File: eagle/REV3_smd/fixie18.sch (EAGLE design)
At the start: 60 parts, among them IC1 74LS595D, IC2 74LS595D, IC3 MEGA8-AI, Q1 CSTCR6M00G53Z

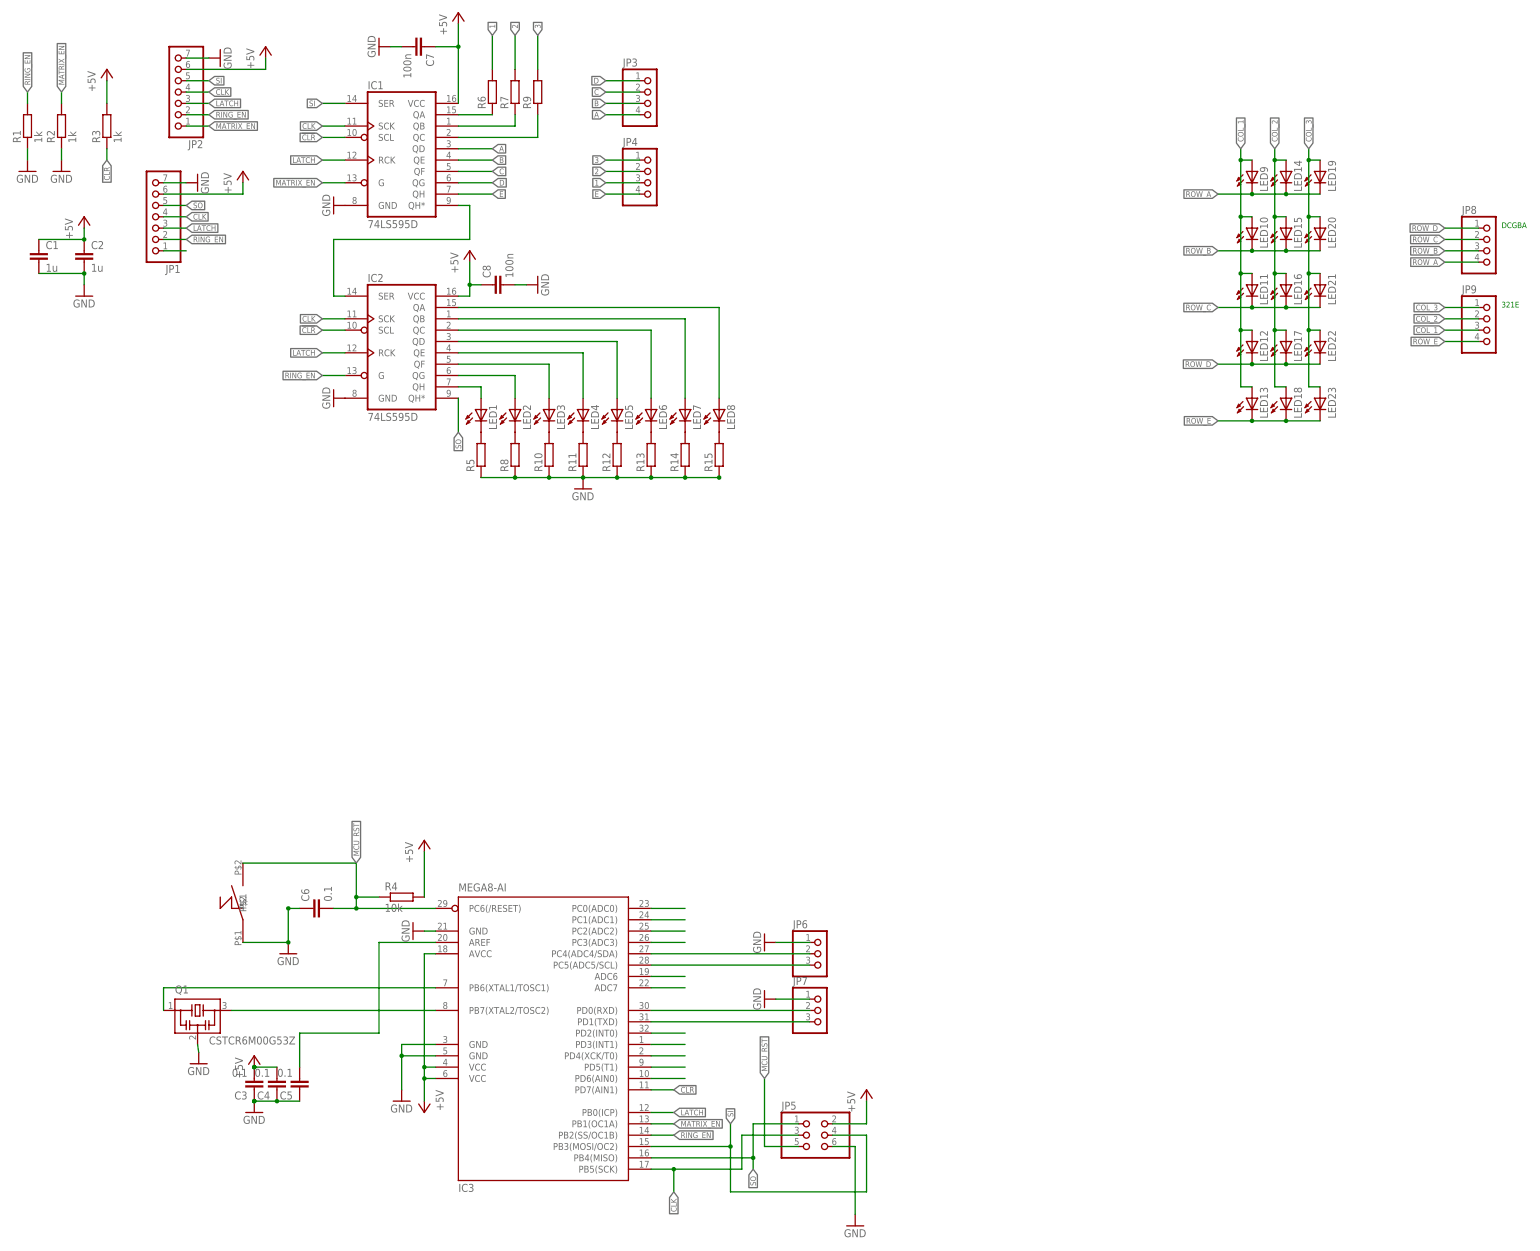
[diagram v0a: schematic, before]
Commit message: Full Rev3 Version by Alex
Used the unfinished rev3 Version to build a one 5x5cm PCB Version. With
some additional Features: second shift-register for Ring LEDs, optional
ATmega8/328 to control one or multiple PCBs.
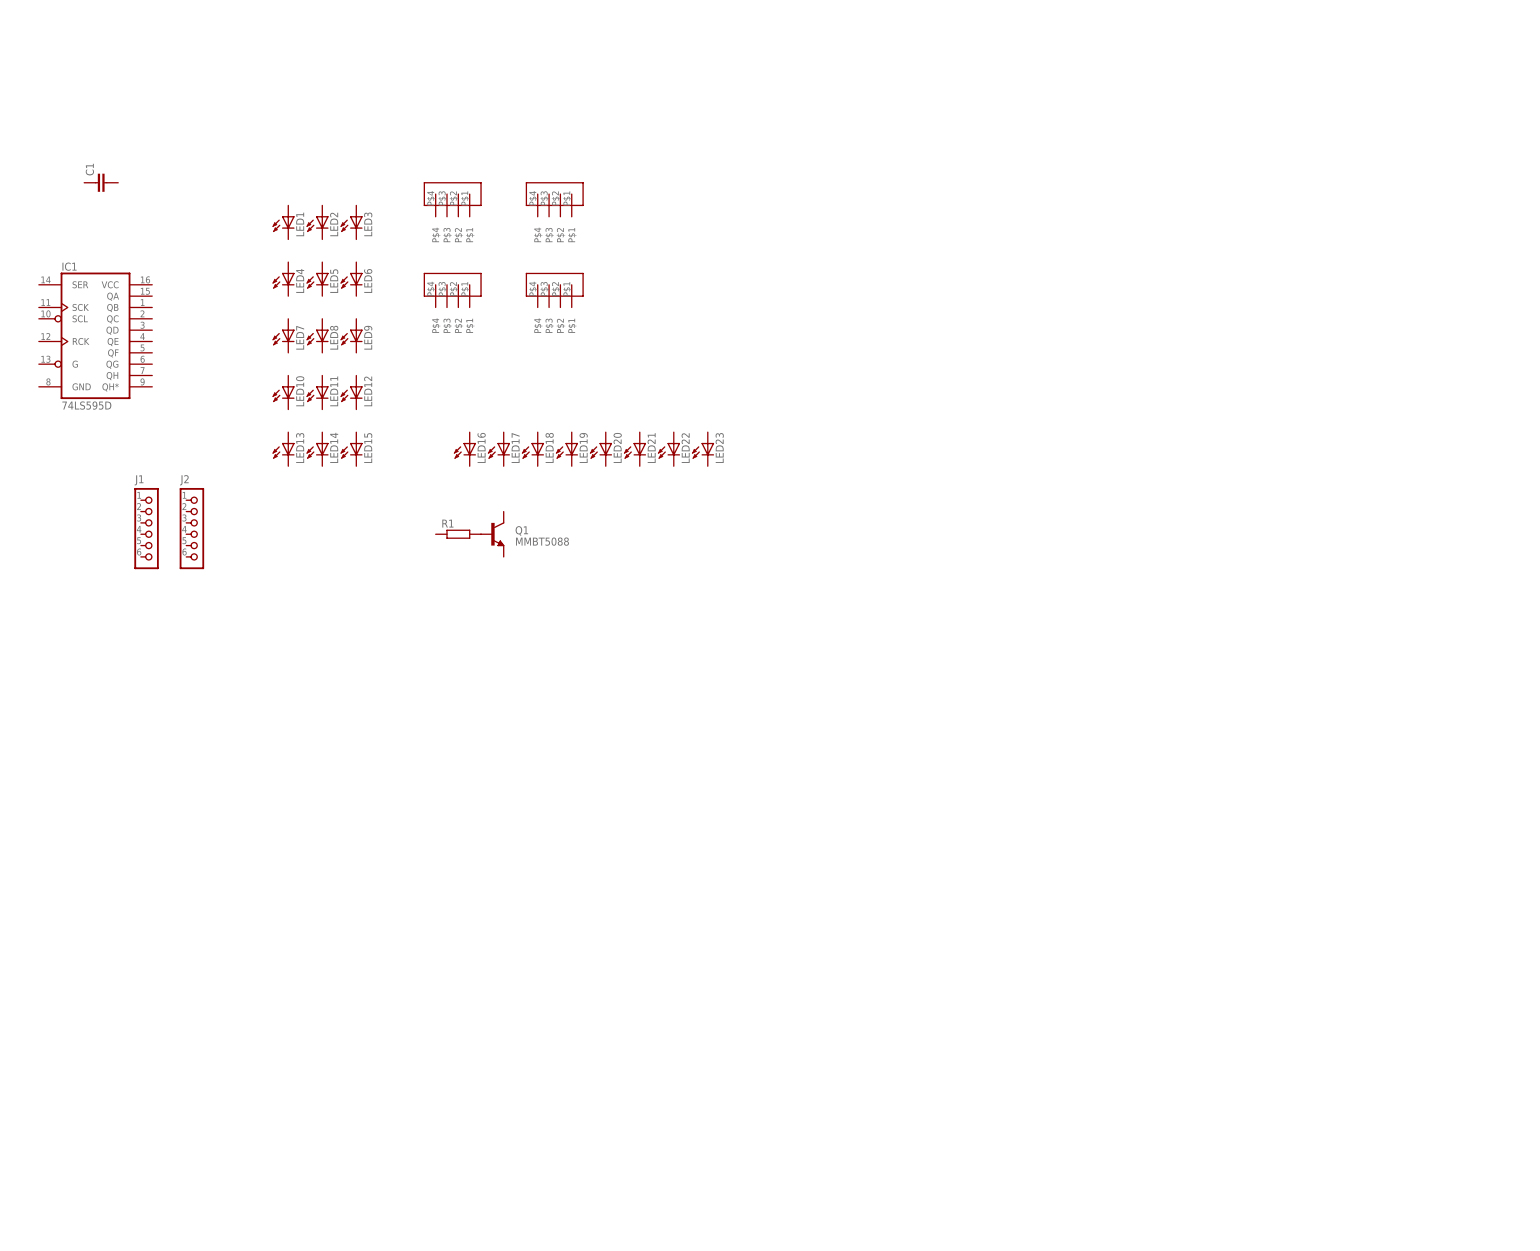
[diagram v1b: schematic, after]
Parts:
- removed C2: 1u, rcl:C-EUC0603-VISHAY
- removed C3, C4, C5, C6: 0.1, rcl:C-EUC0603-VISHAY
- removed C7, C8: 100n, rcl:C-EUC0603-VISHAY
- removed IC2: 74LS595D, SparkFun-DigitalIC:74LS595D
- removed IC3: MEGA8-AI, atmel:MEGA8-AI
- removed JP5: (no value), pinhead:PINHD-2X3
- removed JP6, JP7: (no value), pinhead:PINHD-1X3NOSM
- removed JP8, JP9: (no value), pinhead:PINHD-1X4NOSM
- removed R10, R11, R12, R13, R14, R15, R5, R6, R7, R8, R9: (no value), rcl:R-EU_R0603-VISHAY
- removed R2, R3: 1k, rcl:R-EU_R0603-VISHAY
- removed R4: 10k, rcl:R-EU_R0603-VISHAY
- removed S1: (no value), _miniRoboter:SMD_SWITCH
- added J1, J2: CON_HEADER_1X06-PTH, dp_devices:CON_HEADER_1X06-PTH
- C1: value 1u -> (none); device rcl:C-EUC0603-VISHAY -> rcl:C-EUC1206
- JP1, JP2: value (none) -> HEADER_CENTERED_04; device pinhead:PINHD-1X7RNDNOSILK -> fixie18:HEADER_CENTERED_04
- JP3, JP4: value (none) -> HEADER_CENTERED_04; device pinhead:PINHD-1X4NOSM -> fixie18:HEADER_CENTERED_04
- LED16, LED17, LED18, LED19, LED20, LED21, LED22, LED23: device led:LED3MM -> led:LEDCHIPLED_1206
- Q1: value CSTCR6M00G53Z -> MMBT5088; device murata-filter:CSTCR6M00G53Z -> SparkFun-DiscreteSemi:TRANSISTOR_NPNMMBT5088
- R1: value 1k -> (none); device rcl:R-EU_R0603-VISHAY -> rcl:R-EU_M1206
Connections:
- removed net !CLR: IC1.SCL, IC2.SCL, IC3.PD7(AIN1), R3.1
- removed net +5V: C1.1, C2.1, C3.2, C4.2, C7.1, C8.1, IC1.VCC, IC2.VCC, IC3.AVCC, IC3.VCC@1, IC3.VCC@2, JP1.6, JP2.6, JP5.2, R3.2, R4.2
- removed net 1: JP4.3, R6.2
- removed net 2: JP4.2, R7.2
- removed net 3: JP4.1, R9.2
- removed net A: IC1.QD, JP3.4
- removed net B: IC1.QE, JP3.3
- removed net C: IC1.QF, JP3.2
- removed net CLK: IC1.SCK, IC2.SCK, IC3.PB5(SCK), JP1.4, JP2.4, JP5.3
- removed net COL_1: JP9.3, LED10.A, LED11.A, LED12.A, LED13.A, LED9.A
- removed net COL_2: JP9.2, LED14.A, LED15.A, LED16.A, LED17.A, LED18.A
- removed net COL_3: JP9.1, LED19.A, LED20.A, LED21.A, LED22.A, LED23.A
- removed net D: IC1.QG, JP3.1
- removed net E: IC1.QH, JP4.4
- removed net GND: C1.2, C2.2, C3.1, C4.1, C5.1, C6.1, C7.2, C8.2, IC1.GND, IC2.GND, IC3.GND, IC3.GND@1, IC3.GND@2, JP1.7, JP2.7, JP5.6, JP6.1, JP7.1, Q1.2, R1.1, R10.1, R11.1, R12.1, R13.1, R14.1, R15.1, R2.1, R5.1, R8.1, S1.P$1
- removed net LATCH: IC1.RCK, IC2.RCK, IC3.PB0(ICP), JP1.3, JP2.3
- removed net MATRIX_EN: IC1.G, IC3.PB1(OC1A), JP1.1, JP2.1, R2.2
- removed net MCU_RST: C6.2, IC3.PC6(/RESET), JP5.5, R4.1, S1.P$2
- removed net N$10: IC1.QA, R6.1
- removed net N$11: IC1.QB, R7.1
- removed net N$12: IC1.QC, R9.1
- removed net N$13: LED1.C, R5.2
- removed net N$14: LED2.C, R8.2
- removed net N$15: LED3.C, R10.2
- removed net N$16: LED4.C, R11.2
- removed net N$17: LED5.C, R12.2
- removed net N$18: LED6.C, R13.2
- removed net N$19: LED7.C, R14.2
- removed net N$2: IC2.QH, LED1.A
- removed net N$20: LED8.C, R15.2
- removed net N$21: IC1.QH*, IC2.SER
- removed net N$24: IC3.PD2(INT0)
- removed net N$25: IC3.PD3(INT1)
- removed net N$26: IC3.PD4(XCK/T0)
- removed net N$27: IC3.PD5(T1)
- removed net N$28: IC3.PD6(AIN0)
- removed net N$3: IC2.QG, LED2.A
- removed net N$30: IC3.PC0(ADC0)
- removed net N$31: IC3.PC1(ADC1)
- removed net N$32: IC3.PC2(ADC2)
- removed net N$33: IC3.PC3(ADC3)
- removed net N$36: C5.2, IC3.AREF
- removed net N$38: IC3.ADC6
- removed net N$39: IC3.ADC7
- removed net N$4: IC2.QF, LED3.A
- removed net N$5: IC2.QE, LED4.A
- removed net N$6: IC2.QD, LED5.A
- removed net N$7: IC2.QC, LED6.A
- removed net N$8: IC2.QB, LED7.A
- removed net N$9: IC2.QA, LED8.A
- removed net PB6: IC3.PB6(XTAL1/TOSC1), Q1.1
- removed net PB7: IC3.PB7(XTAL2/TOSC2), Q1.3
- removed net RING_EN: IC2.G, IC3.PB2(SS/OC1B), JP1.2, JP2.2, R1.2
- removed net ROW_A: JP8.4, LED14.C, LED19.C, LED9.C
- removed net ROW_B: JP8.3, LED10.C, LED15.C, LED20.C
- removed net ROW_C: JP8.2, LED11.C, LED16.C, LED21.C
- removed net ROW_D: JP8.1, LED12.C, LED17.C, LED22.C
- removed net ROW_E: JP9.4, LED13.C, LED18.C, LED23.C
- removed net RX: IC3.PD0(RXD), JP7.2
- removed net SCL: IC3.PC5(ADC5/SCL), JP6.3
- removed net SDA: IC3.PC4(ADC4/SDA), JP6.2
- removed net SI: IC1.SER, IC3.PB3(MOSI/OC2), JP2.5, JP5.4
- removed net SO: IC2.QH*, IC3.PB4(MISO), JP1.5, JP5.1
- removed net TX: IC3.PD1(TXD), JP7.3
- new net N$1: Q1.B, R1.2
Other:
- note removed: "321E"
- note removed: "DCGBA"
- moved on the sheet: C1, IC1, LED1, LED10, LED11, LED12, LED13, LED14, LED15, LED16, LED17, LED18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
